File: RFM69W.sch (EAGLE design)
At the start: 18 parts, among them U1 RFM69W, U2 MCP1701

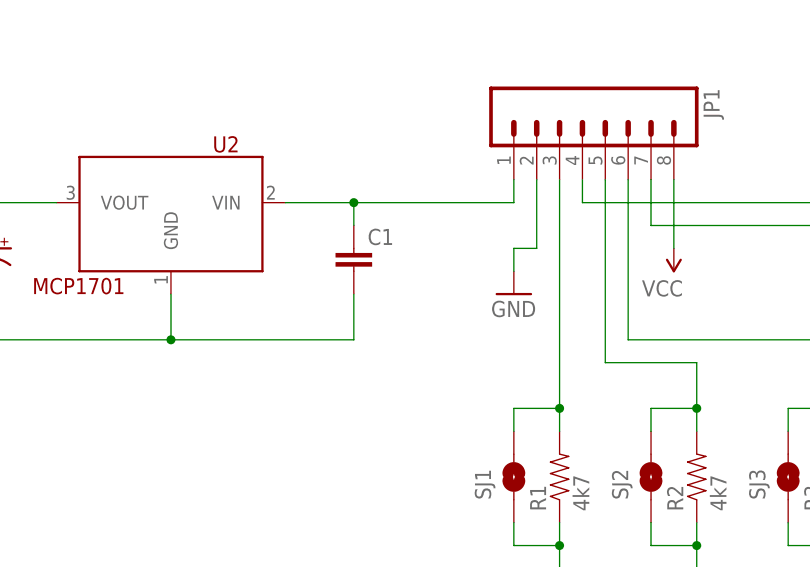
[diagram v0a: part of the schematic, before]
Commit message: Updated README to confirm tested
Also filled in value on bypass cap.
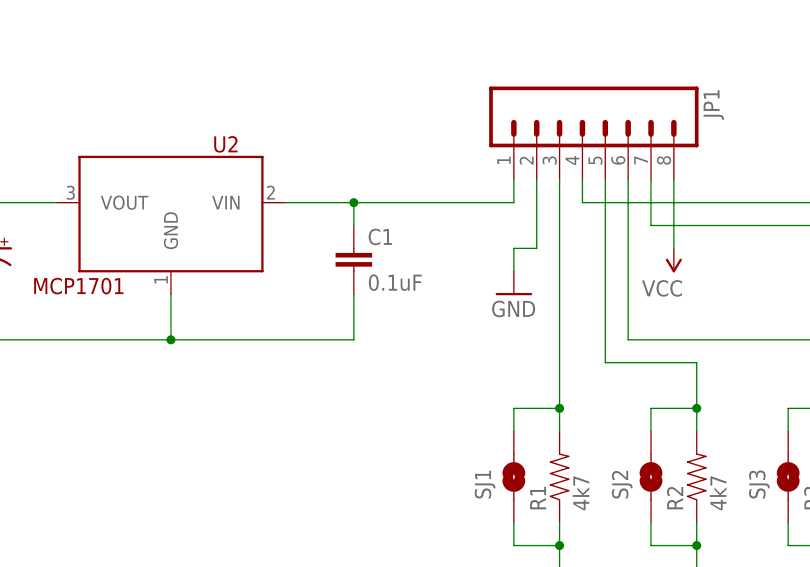
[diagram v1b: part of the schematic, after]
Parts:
- C1: value (none) -> 0.1uF
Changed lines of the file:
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@@
 <part name="R5" library="SparkFun-Resistors" deviceset="RESISTOR" device="0805-RES" value="10k"/>
 <part name="R6" library="SparkFun-Resistors" deviceset="RESISTOR" device="0805-RES" value="10k"/>
-<part name="C1" library="SparkFun-Capacitors" deviceset="CAP" device="0805"/>
+<part name="C1" library="SparkFun-Capacitors" deviceset="CAP" device="0805" value="0.1uF"/>
 <part name="C2" library="SparkFun-Capacitors" deviceset="CAP" device="0805" value="0.1uF"/>
 <part name="SJ1" library="SparkFun-Passives" deviceset="SOLDERJUMPER" device="NO" value=""/>
